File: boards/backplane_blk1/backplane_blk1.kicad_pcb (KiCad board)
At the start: 4 copper layers, 246.4 x 151.1 mm, 10 parts, among them J1 DIN41612_03x32_C, J2 Conn_04x22

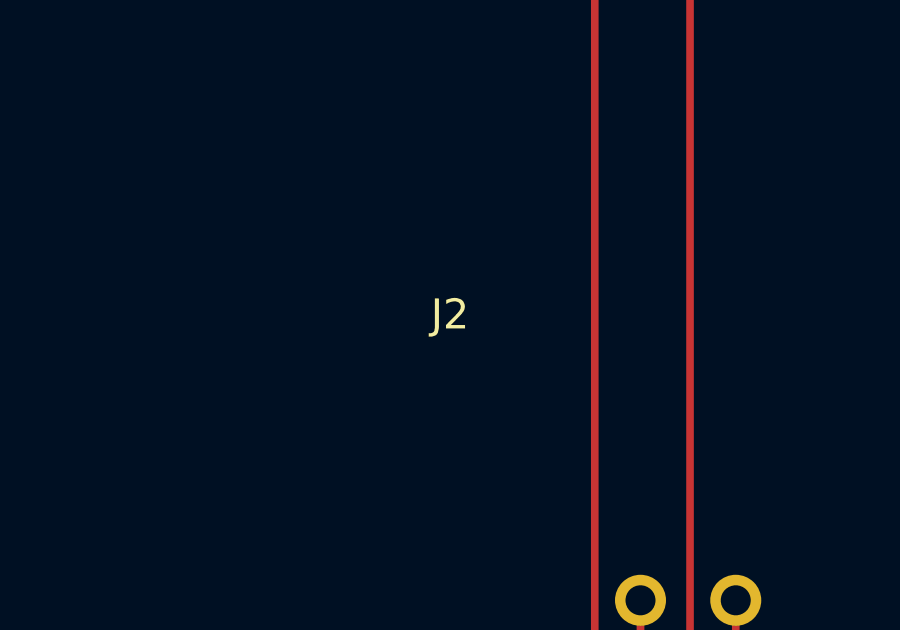
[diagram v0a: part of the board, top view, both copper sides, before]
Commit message: Block I: finished up the first pass on the backplane
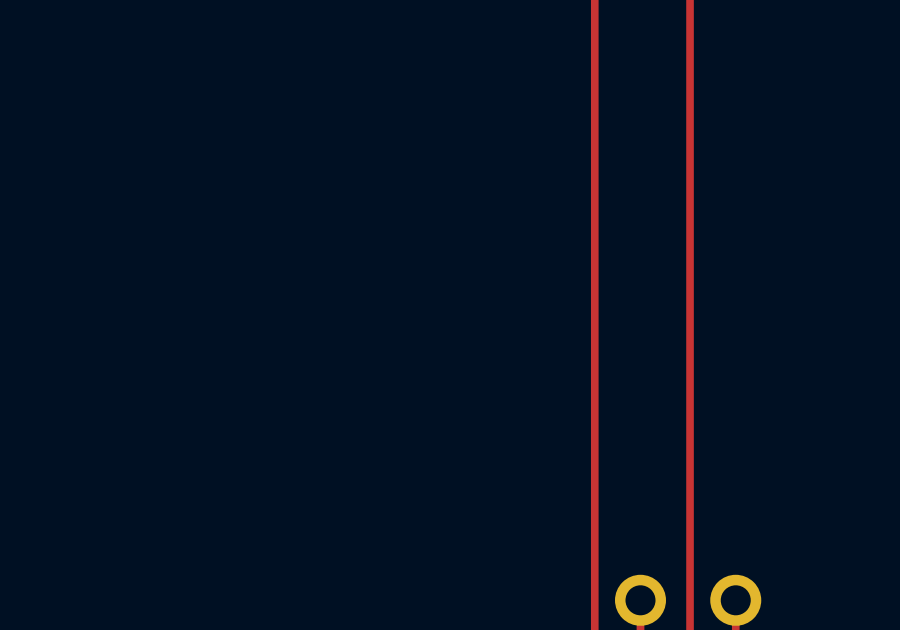
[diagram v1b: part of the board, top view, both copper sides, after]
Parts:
- added G***: LOGO, lachesis:big_cores, B.Cu at (199.8, 150.6)
- added G***: LOGO, lachesis:big_rope_curve, B.Cu at (199.8, 76.1)
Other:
- board text added: "01"
- board text added: "02"
- board text added: "03"
- board text added: "04"
- board text added: "05"
- board text added: "06"
- board text added: "07"
- board text added: "08"
- board text added: "09"
- board text added: "1"
- board text added: "10"
- board text added: "11"
- board text added: "12"
- board text added: "13"
- board text added: "14"
- board text added: "15"
- board text added: "16"
- board text added: "17"
- board text added: "18"
- board text added: "19"
- board text added: "20"
- board text added: "21"
- board text added: "22"
- board text added: "23"
- board text added: "24"
- board text added: "25"
- board text added: "26"
- board text added: "27"
- board text added: "28"
- board text added: "29"
- board text added: "30"
- board text added: "31"
- board text added: "32"
- board text added: "33"
- board text added: "37"
- board text added: "41"
- board text added: "45"
- board text added: "49"
- board text added: "5"
- board text added: "53"
- board text added: "57"
- board text added: "61"
- board text added: "65"
- board text added: "69"
- board text added: "73"
- board text added: "77"
- board text added: "81"
- board text added: "85"
- board text added: "A"
- board text added: "B"
- board text added: "C"
- board text added: "Mike Stewart 2022"
